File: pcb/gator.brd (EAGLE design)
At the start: 101.6 x 81.3 mm, 78 parts, among them J2 POWER_JACKPTH, X1 USB-A-S, Y1 12MHz

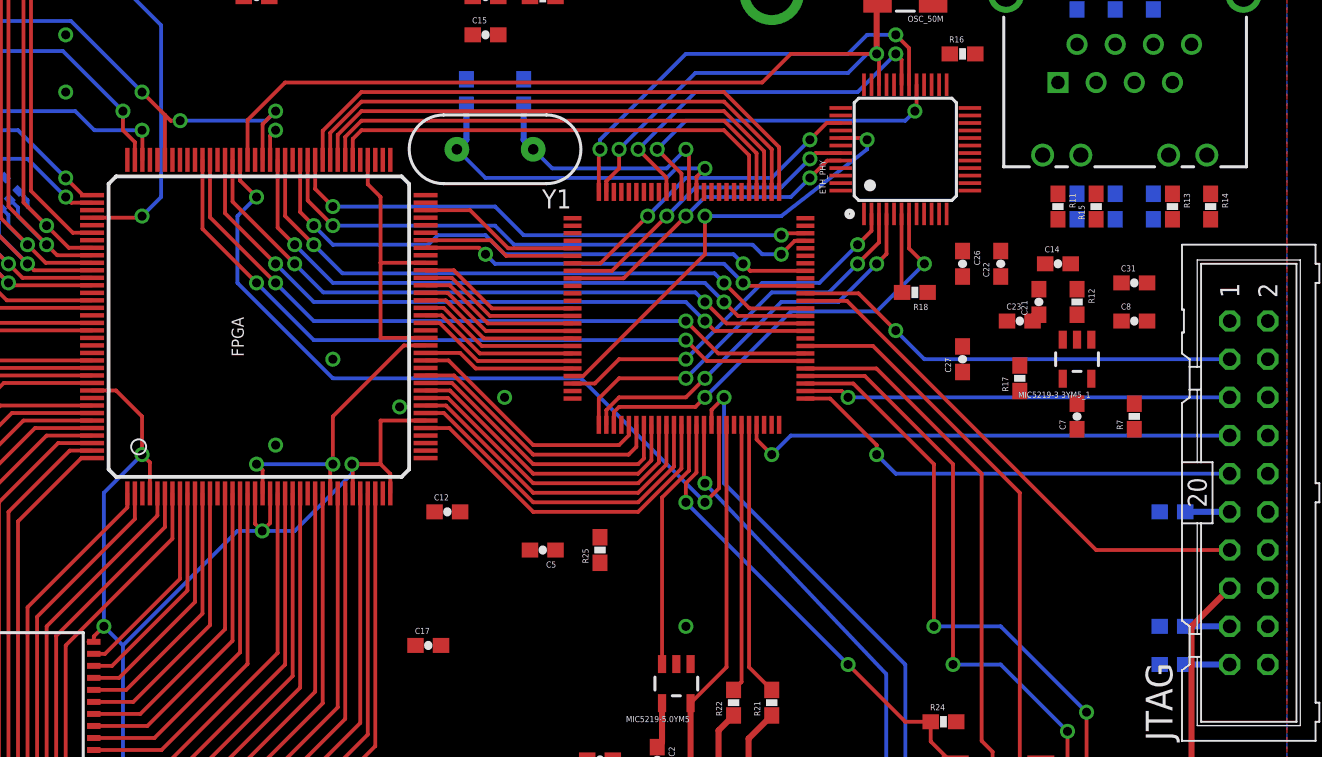
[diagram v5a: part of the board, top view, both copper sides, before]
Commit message: Finished routing power for FPGA and microcontroller
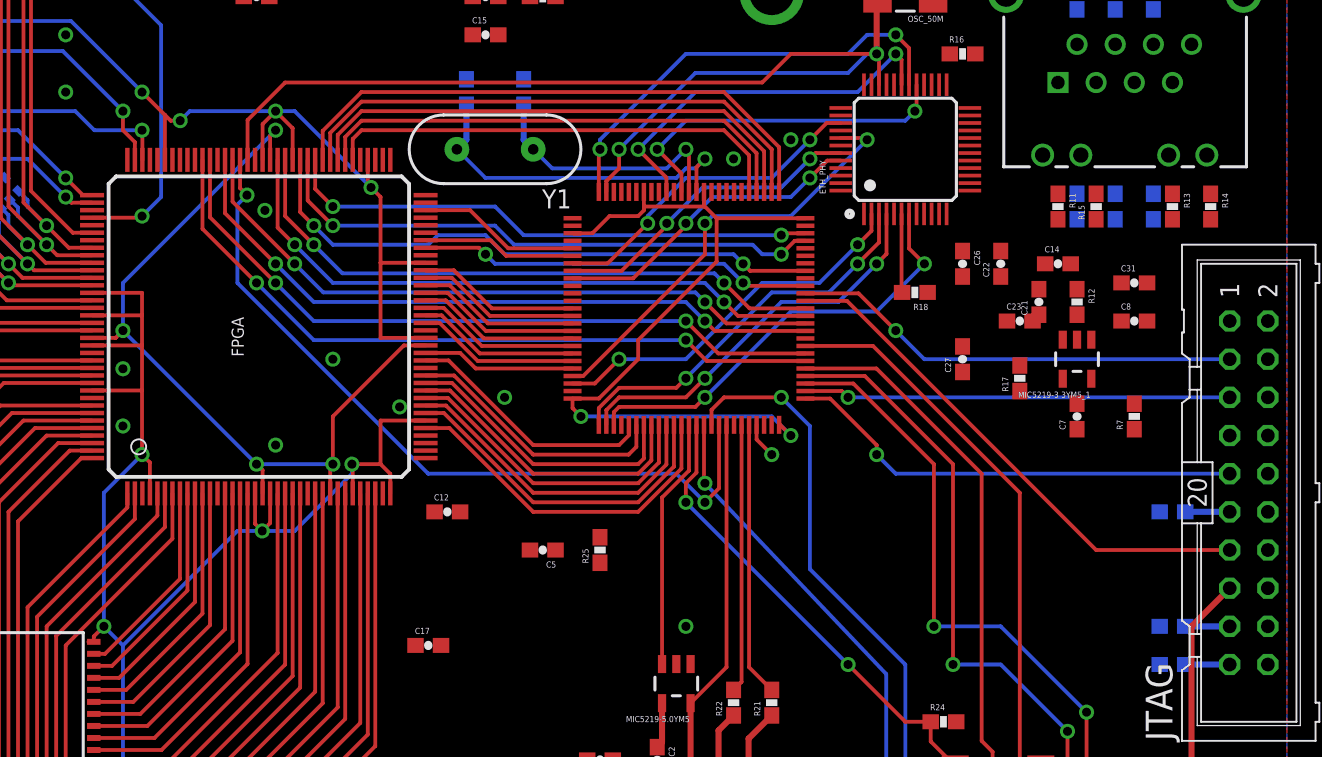
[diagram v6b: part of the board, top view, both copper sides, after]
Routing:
- net VDD: track 0.00 -> 53.6 mm, vias 0 -> 2
- net VCCINT: track 22.6 -> 55.0 mm, vias 3 -> 4
- net TMS/SWDIO: track 33.4 -> 2.40 mm
- net VCCIO: track 170.4 -> 200.1 mm, vias 12 -> 13
- net SD_D1: track 43.0 -> 45.3 mm
- net N$29: track 22.6 -> 23.5 mm
- net FPGA_CLK1: track 51.9 -> 51.4 mm

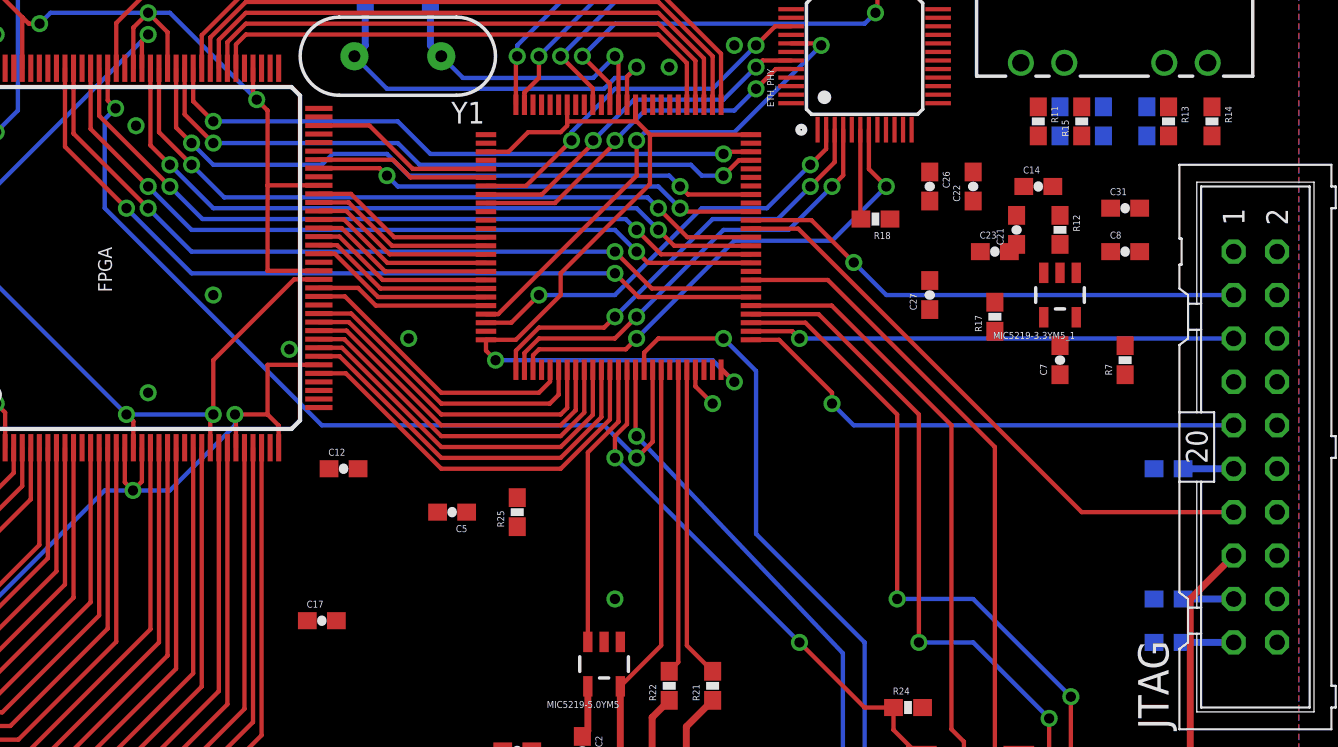
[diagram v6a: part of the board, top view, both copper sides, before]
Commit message: Added INIT_B and PROGRAM_B signals needed for slave serial configuration
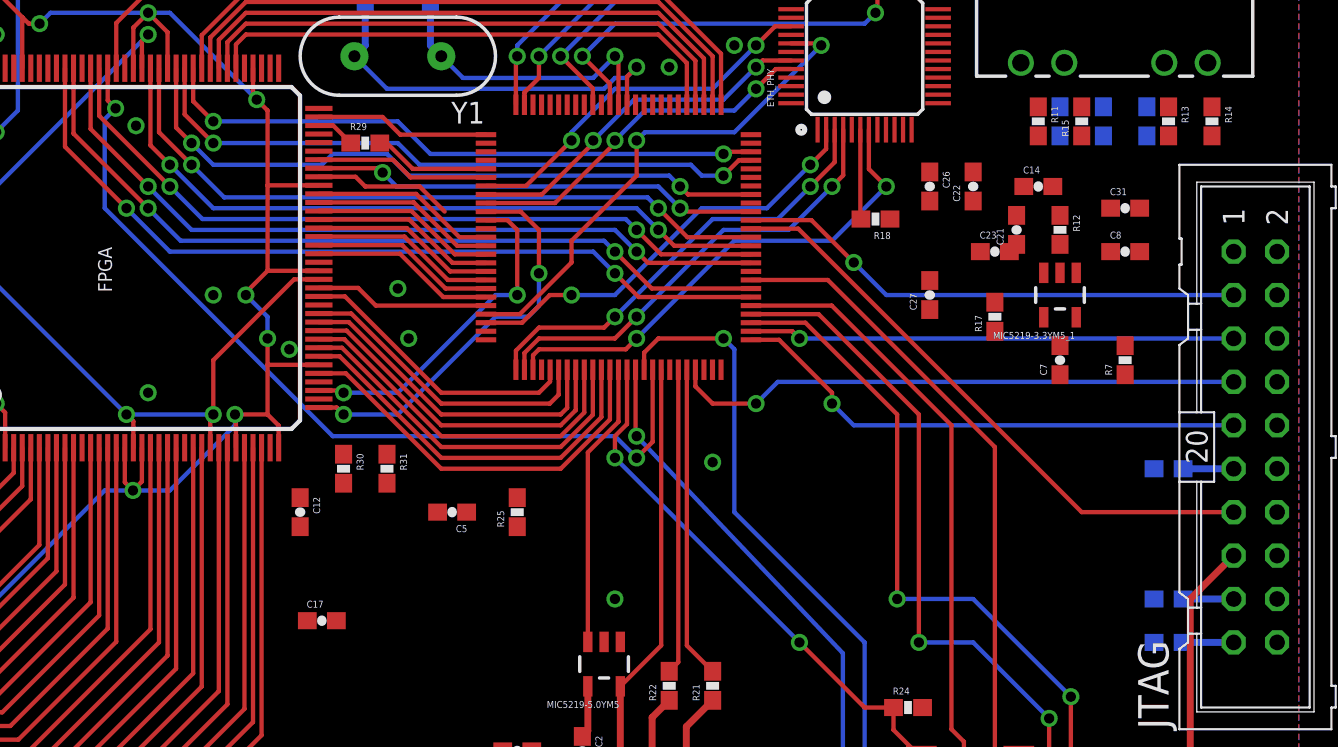
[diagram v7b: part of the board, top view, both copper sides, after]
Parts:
- added R29: 50, SparkFun-Passives:0603-RES
- added R30, R31: 4K7, SparkFun-Passives:0603-RES
- moved C12 3.59 mm to (40.6, 30.5), turned to 270 degrees
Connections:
- removed net CSO_B: FPGA.P38
- removed net VDD: U$1.100, U$1.11, U$1.19, U$1.28, U$1.50, U$1.75
- new net N$33: FPGA.P70, R29.1
- new net VSYNC: FPGA.P64
- net +3V3: now also R30.2, R31.2, U$1.100, U$1.11, U$1.19, U$1.28, U$1.50, U$1.75
- net CFG_CLK: now also R29.2; no longer FPGA.P70
- net DONE: now also U$1.26
- net INIT_B: now also R31.1, U$1.36
- net PROGRAM_B: now also R30.1, U$1.35
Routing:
- net VDD: track 53.6 -> 0.00 mm, vias 2 -> 0
- net TMS/SWDIO: track 2.40 -> 33.4 mm
- net PROGRAM_B: track 0.00 -> 23.7 mm, vias 0 -> 2
- net INIT_B: track 0.00 -> 19.9 mm, vias 0 -> 2
- net DONE: track 0.00 -> 10.2 mm
- net VSYNC: track 0.00 -> 8.20 mm
- net VCCIO: track 200.1 -> 206.6 mm, vias 13 -> 15
- net CFG_CLK: track 10.8 -> 6.84 mm
- net N$33: track 0.00 -> 2.29 mm
- net MII_RX_ER: track 29.1 -> 29.9 mm

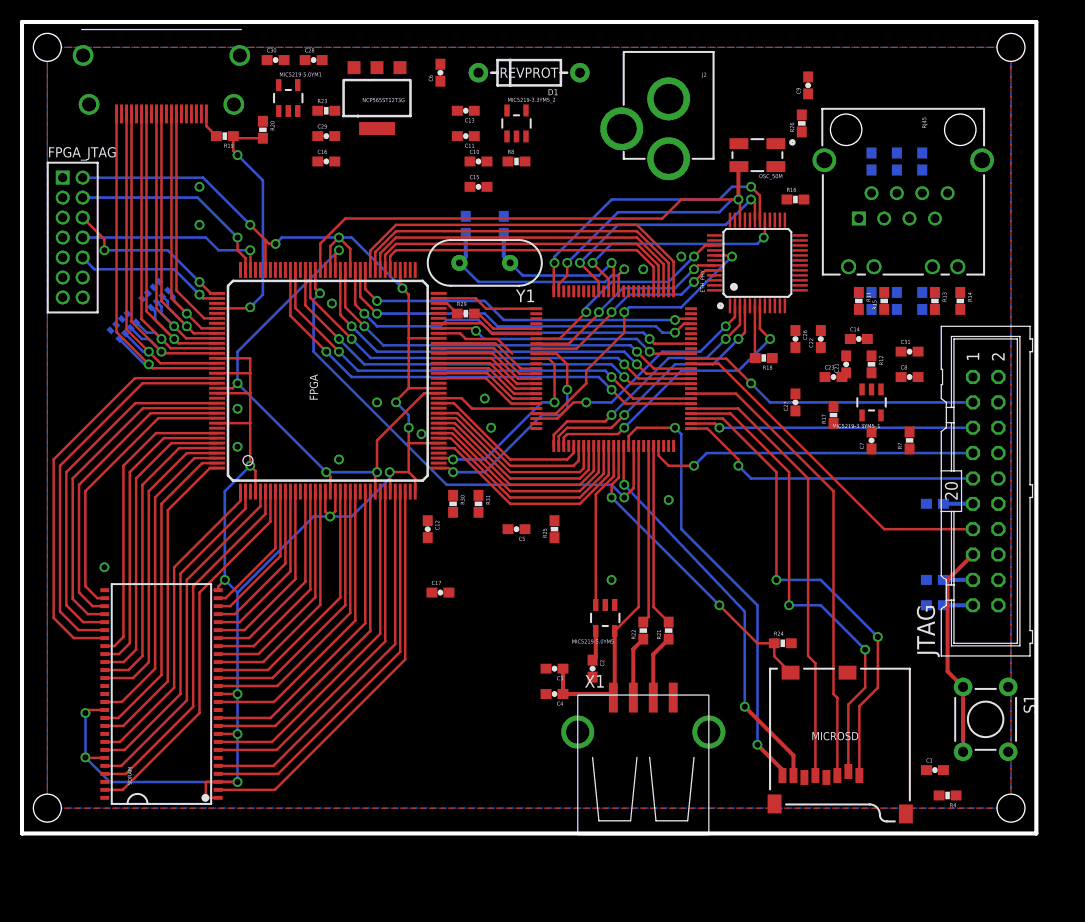
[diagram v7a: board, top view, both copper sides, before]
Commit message: Routed power to ARM, added VSync signal
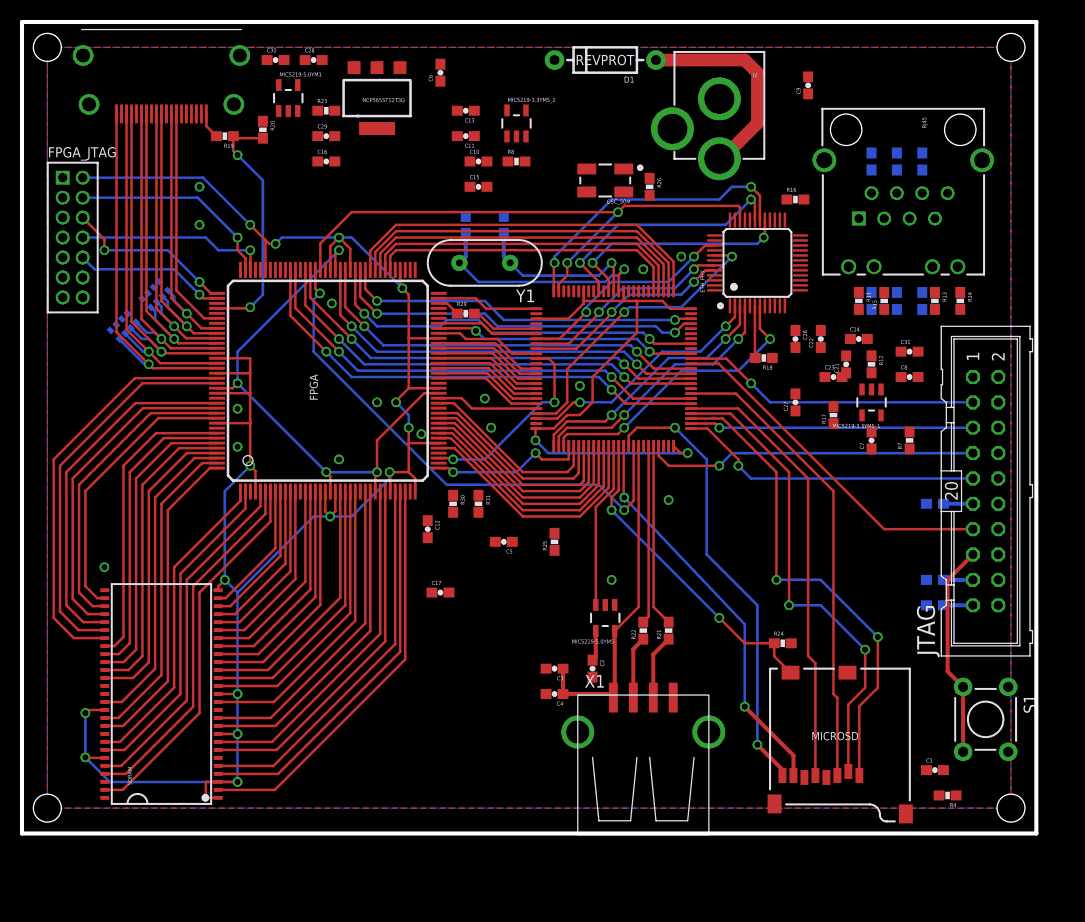
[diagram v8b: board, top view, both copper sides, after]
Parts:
- moved R26 16.5 mm to (62.9, 64.8), turned to 270 degrees
- moved OSC_50M 15.5 mm to (58.4, 65.4)
- moved D1 7.73 mm to (58.4, 77.5)
- moved J2 5.08 mm to (69.8, 81.3)
- moved C5 1.80 mm to (48.3, 29.2)
- moved R25 1.27 mm to (53.3, 29.2)
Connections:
- net PROGRAM_B: now also U$1.54; no longer U$1.35
- net VSYNC: now also U$1.35
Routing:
- net +3V3: track 0.00 -> 56.1 mm, vias 0 -> 2
- net N$3: track 0.00 -> 21.0 mm
- net 50MHZ_OSC: track 74.7 -> 57.9 mm
- net PROGRAM_B: track 23.7 -> 15.6 mm
- net VSYNC: track 8.20 -> 10.6 mm
- net FPGA_CLK1: track 51.4 -> 53.1 mm
- net D0: track 22.8 -> 24.5 mm
- net D13: track 16.8 -> 18.6 mm
- net D1: track 23.4 -> 25.2 mm
- net A16: track 20.1 -> 21.9 mm
- net D15: track 19.2 -> 21.0 mm
- net D14: track 17.9 -> 19.7 mm
- net A18: track 21.9 -> 23.6 mm
- net A17: track 21.0 -> 22.8 mm
- net SD_DETECT: track 31.4 -> 32.2 mm
